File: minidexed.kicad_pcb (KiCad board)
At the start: 2 copper layers, 130.8 x 85 mm, 53 parts, among them J1 Audio Out, J2 MIDI In, J3 Raspberry_Pi_2_3, J4 MIDI Thru, J5 MIDI Out, J6 GND TP, SW1 Encoder, SW2 B1, SW3 B2, SW4 B3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

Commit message: rough out tracks
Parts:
- U3: footprint Package_SO:TSSOP-14_4.4x3.6mm_P0.4mm -> Package_SO:TSSOP-14_4.4x5mm_P0.65mm
- moved R2 14.4 mm to (197.5, 107.0)
- moved R5 14.1 mm to (183.2, 107.0)
- moved J6 9.05 mm to (160.3, 104.3)
- moved C15 5.41 mm to (148.6, 73.1)
- moved R4 4.50 mm to (153.5, 73.1)
- moved TP6 4.14 mm to (151.9, 87.5)
- moved TP5 2.34 mm to (143.8, 81.9)
- moved U3 0.92 mm to (125.7, 87.0)
- moved TP8 0.50 mm to (143.0, 88.0)
- moved R3 0.25 mm to (190.3, 107.0)
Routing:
- net +5V: track 0.00 -> 214.1 mm, vias 0 -> 5
- net +3.3V: track 0.00 -> 202.6 mm, vias 0 -> 3
- net /LCD_E: track 0.00 -> 156.8 mm
- net /BTN_1: track 0.00 -> 114.6 mm
- net /BTN_2: track 0.00 -> 96.0 mm
- net /MIDI_RX: track 0.00 -> 89.6 mm
- net /LCD_RS: track 0.00 -> 86.9 mm, vias 0 -> 1
- net /LCD_D4: track 0.00 -> 69.5 mm
- net /MIDI_TX: track 0.00 -> 69.5 mm
- net /LCD_D5: track 0.00 -> 62.1 mm
- net /LCD_D6: track 0.00 -> 58.1 mm
- net /LCD_D7: track 0.00 -> 52.3 mm, vias 0 -> 1
- net /DAC_A_3V3: track 0.00 -> 51.1 mm, vias 0 -> 2
- net /ENC_A_CLK: track 0.00 -> 39.7 mm
- net /ENC_B_DT: track 0.00 -> 39.2 mm
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- added copper zone on B.Cu, net GND
- added copper zone on F.Cu, net GND
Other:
- rule pad_to_mask_clearance: 0 -> 0.05

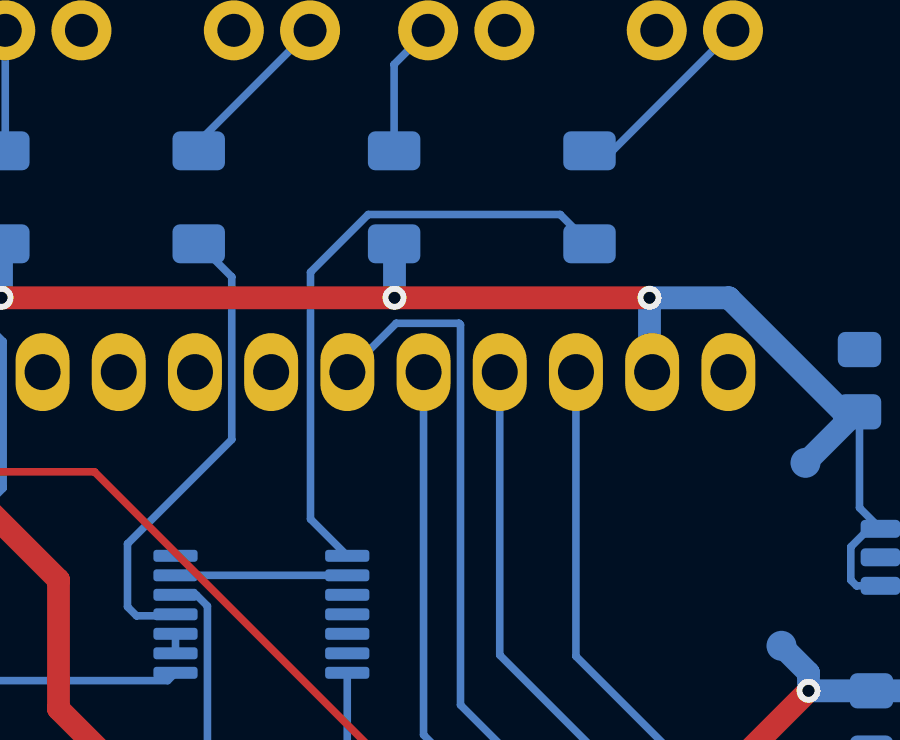
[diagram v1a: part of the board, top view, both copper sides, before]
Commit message: add image errors
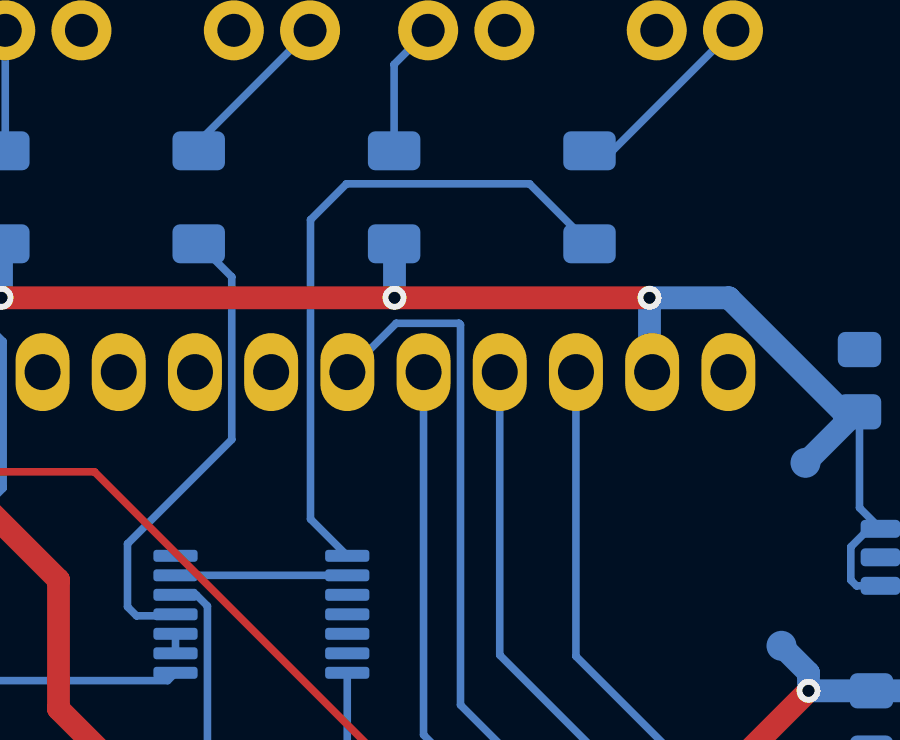
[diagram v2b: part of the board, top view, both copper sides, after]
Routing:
- net Net-(R11-Pad2): track 20.5 -> 22.3 mm
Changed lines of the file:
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@@
   (segment (start 124.675 75.70092) (end 124.675 81.125) (width 0.254) (layer "B.Cu") (net 57))
   (segment (start 121.5 87) (end 122.75 87) (width 0.254) (layer "B.Cu") (net 57))
-  (segment (start 129.223039 73.623) (end 127.3 75.546039) (width 0.254) (layer "B.Cu") (net 58))
-  (segment (start 136.6 74.6) (end 135.623 73.623) (width 0.254) (layer "B.Cu") (net 58))
-  (segment (start 127.3 75.546039) (end 127.3 83.775) (width 0.254) (layer "B.Cu") (net 58))
-  (segment (start 127.3 83.775) (end 128.525 85) (width 0.254) (layer "B.Cu") (net 58))
-  (segment (start 135.623 73.623) (end 129.223039 73.623) (width 0.254) (layer "B.Cu") (net 58))
+  (segment (start 127.3 73.8) (end 128.5 72.6) (width 0.254) (layer "B.Cu") (net 58))
+  (segment (start 127.3 83.775) (end 127.3 73.8) (width 0.254) (layer "B.Cu") (net 58))
+  (segment (start 128.5 72.6) (end 134.6 72.6) (width 0.254) (layer "B.Cu") (net 58))
+  (segment (start 134.6 72.6) (end 136.6 74.6) (width 0.254) (layer "B.Cu") (net 58))
+  (segment (start 128.525 85) (end 127.3 83.775) (width 0.254) (layer "B.Cu") (net 58))
   (segment (start 122.8 87.6) (end 122.8 88.25) (width 0.254) (layer "B.Cu") (net 60))
   (segment (start 128.525 85.65) (end 122.8 85.65) (width 0.254) (layer "B.Cu") (net 61))

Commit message: fix gnd issue
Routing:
- net GND: vias 18 -> 13

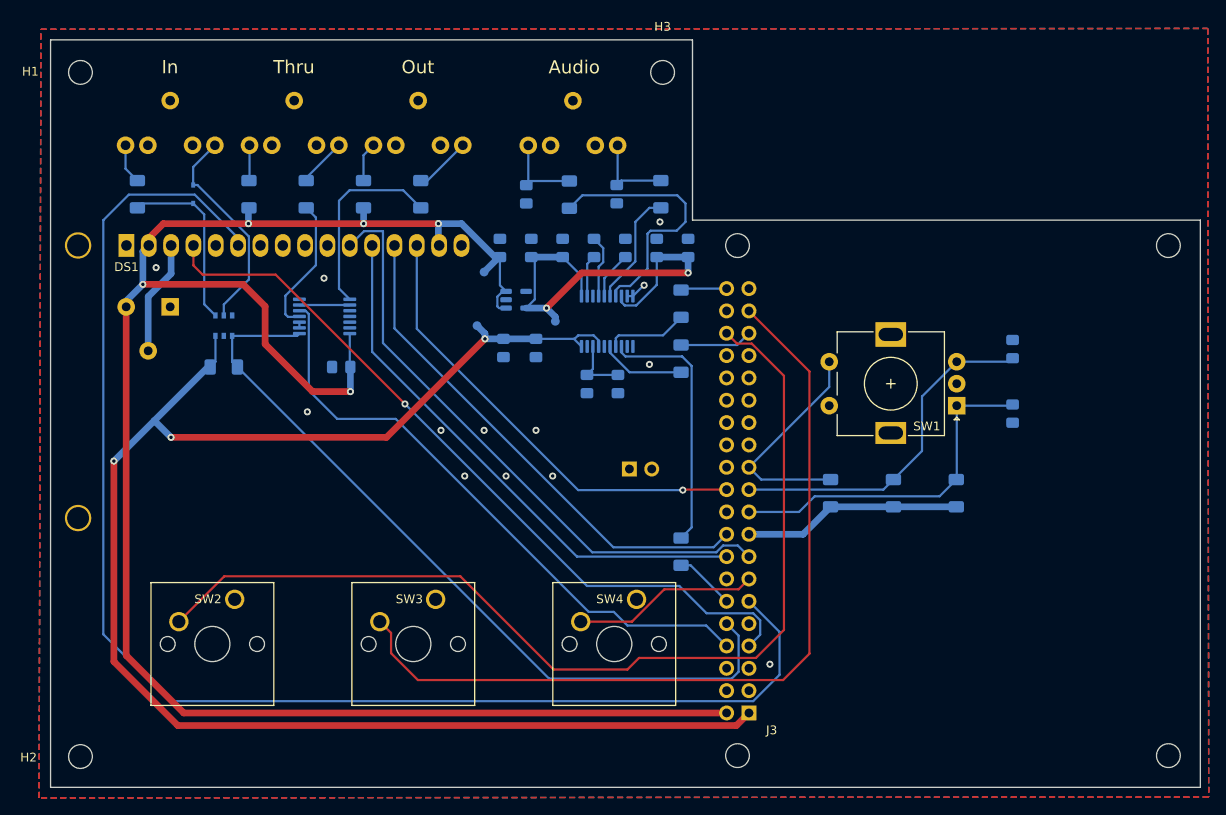
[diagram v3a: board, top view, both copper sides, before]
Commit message: fix missing GND connection
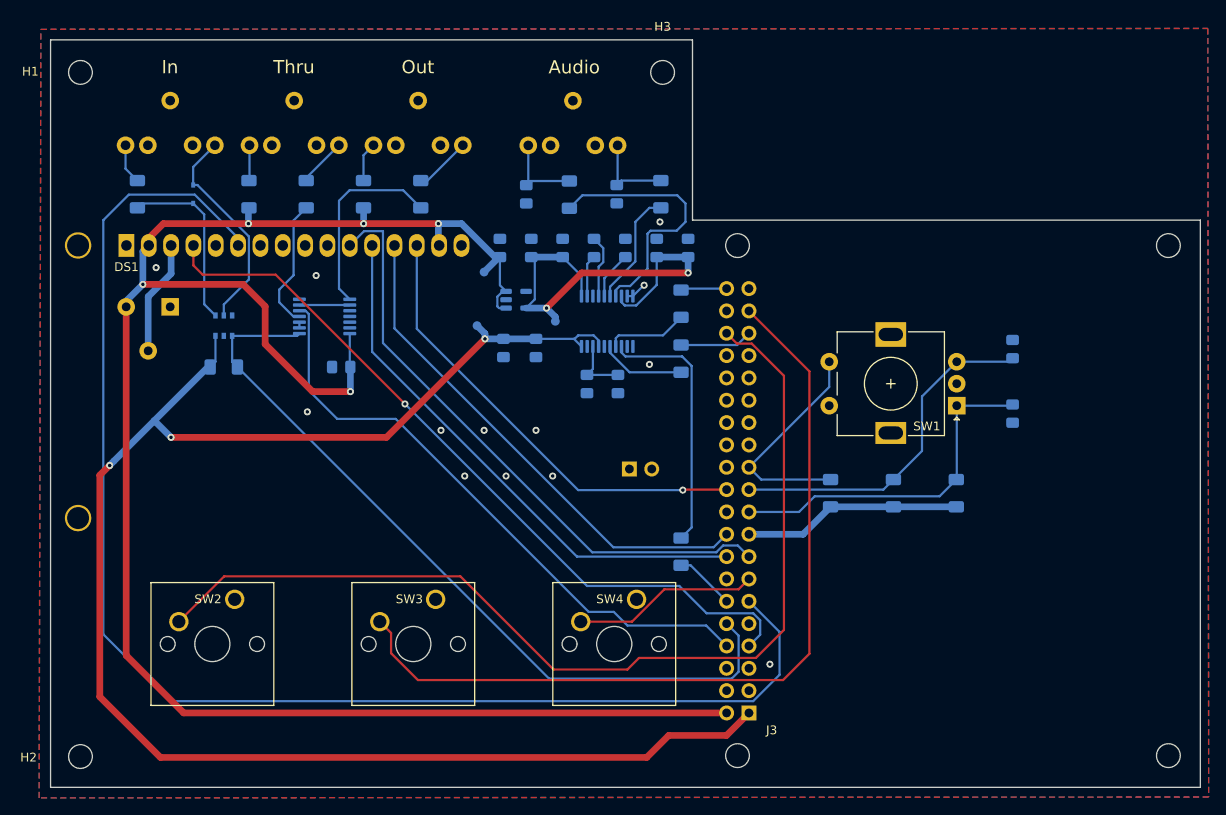
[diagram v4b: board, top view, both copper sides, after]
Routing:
- net +3.3V: track 202.6 -> 210.2 mm
- net Net-(R10-Pad2): track 15.7 -> 15.0 mm
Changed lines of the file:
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@@
   (segment (start 105 83.3) (end 105 79.5445) (width 0.762) (layer "B.Cu") (net 1))
   (segment (start 103.1 85.86) (end 103.1 85.2) (width 0.762) (layer "B.Cu") (net 1))
+  (via (at 124.7 82.3) (size 0.8) (drill 0.4) (layers "F.Cu" "B.Cu") (free) (net 2))
   (via (at 162 83.4) (size 0.8) (drill 0.4) (layers "F.Cu" "B.Cu") (free) (net 2))
   (via (at 151.6 105.1) (size 0.8) (drill 0.4) (layers "F.Cu" "B.Cu") (free) (net 2))
@@
   (via (at 141.6 105.1) (size 0.8) (drill 0.4) (layers "F.Cu" "B.Cu") (free) (net 2))
   (via (at 146.3 105.1) (size 0.8) (drill 0.4) (layers "F.Cu" "B.Cu") (free) (net 2))
-  (via (at 125.6 82.6) (size 0.8) (drill 0.4) (layers "F.Cu" "B.Cu") (free) (net 2))
   (via (at 138.9 99.9) (size 0.8) (drill 0.4) (layers "F.Cu" "B.Cu") (free) (net 2))
   (segment (start 160.725 84.6375) (end 160.075 84.6375) (width 0.254) (layer "B.Cu") (net 2))
@@
   (segment (start 163.43333 80.2) (end 167 80.2) (width 0.762) (layer "B.Cu") (net 3))
   (segment (start 154.875 82.341668) (end 152.733332 80.2) (width 0.254) (layer "B.Cu") (net 3))
+  (segment (start 173.9184 132.0424) (end 171.3608 134.6) (width 0.762) (layer "F.Cu") (net 4))
+  (segment (start 101.2265 103.9) (end 101.2 103.9) (width 0.762) (layer "F.Cu") (net 4))
+  (segment (start 164.8 134.6) (end 162.3 137.1) (width 0.762) (layer "F.Cu") (net 4))
   (segment (start 132.7 100.7) (end 143.9 89.5) (width 0.762) (layer "F.Cu") (net 4))
-  (segment (start 173.9184 132.0424) (end 172.4874 133.4734) (width 0.762) (layer "F.Cu") (net 4))
-  (segment (start 101.7 126.2) (end 108.9734 133.4734) (width 0.762) (layer "F.Cu") (net 4))
-  (segment (start 101.7 126.2) (end 101.7 103.4) (width 0.762) (layer "F.Cu") (net 4))
-  (segment (start 172.4874 133.4734) (end 108.9734 133.4734) (width 0.762) (layer "F.Cu") (net 4))
+  (segment (start 101.2 103.9) (end 100.1 105) (width 0.762) (layer "F.Cu") (net 4))
+  (segment (start 100.1 130.2) (end 100.1 105) (width 0.762) (layer "F.Cu") (net 4))
+  (segment (start 162.3 137.1) (end 107 137.1) (width 0.762) (layer "F.Cu") (net 4))
+  (segment (start 171.3608 134.6) (end 164.8 134.6) (width 0.762) (layer "F.Cu") (net 4))
+  (segment (start 107 137.1) (end 100.1 130.2) (width 0.762) (layer "F.Cu") (net 4))
   (segment (start 108.2 100.7) (end 132.7 100.7) (width 0.762) (layer "F.Cu") (net 4))
   (via (at 108.2 100.7) (size 0.8) (drill 0.4) (layers "F.Cu" "B.Cu") (net 4))
-  (via (at 101.7 103.4) (size 0.8) (drill 0.4) (layers "F.Cu" "B.Cu") (net 4))
+  (via (at 101.2265 103.9) (size 0.8) (drill 0.4) (layers "F.Cu" "B.Cu") (net 4))
   (via (at 143.9 89.5) (size 0.8) (drill 0.4) (layers "F.Cu" "B.Cu") (net 4))
   (segment (start 113.25 89.16) (end 113.25 92.1) (width 0.254) (layer "B.Cu") (net 4))
@@
   (segment (start 106.3 98.8) (end 112.4 92.7) (width 0.762) (layer "B.Cu") (net 4))
   (segment (start 146 89.5) (end 149.7 89.5) (width 0.762) (layer "B.Cu") (net 4))
+  (segment (start 101.7 103.4) (end 101.2265 103.8735) (width 0.762) (layer "B.Cu") (net 4))
   (segment (start 190.35 108.6) (end 197.5 108.6) (width 0.762) (layer "B.Cu") (net 4))
+  (segment (start 101.2265 103.8735) (end 101.2265 103.9) (width 0.762) (layer "B.Cu") (net 4))
   (segment (start 183.2 108.6) (end 190.35 108.6) (width 0.762) (layer "B.Cu") (net 4))
   (segment (start 143.9 88.9) (end 143 88) (width 0.762) (layer "B.Cu") (net 4))
@@
   (segment (start 158.775 89.425131) (end 158.775 90.3625) (width 0.254) (layer "B.Cu") (net 56))
   (segment (start 159.100131 89.1) (end 158.775 89.425131) (width 0.254) (layer "B.Cu") (net 56))
-  (segment (start 121.2 84.6) (end 121.2 86.7) (width 0.254) (layer "B.Cu") (net 57))
-  (segment (start 121.2 86.7) (end 121.5 87) (width 0.254) (layer "B.Cu") (net 57))
-  (segment (start 123.57408 74.6) (end 124.675 75.70092) (width 0.254) (layer "B.Cu") (net 57))
-  (segment (start 124.675 81.125) (end 121.2 84.6) (width 0.254) (layer "B.Cu") (net 57))
-  (segment (start 124.675 75.70092) (end 124.675 81.125) (width 0.254) (layer "B.Cu") (net 57))
-  (segment (start 121.5 87) (end 122.75 87) (width 0.254) (layer "B.Cu") (net 57))
+  (segment (start 120.5 83.9) (end 120.5 85.341369) (width 0.254) (layer "B.Cu") (net 57))
+  (segment (start 122.135 76.03908) (end 122.135 82.265) (width 0.254) (layer "B.Cu") (net 57))
+  (segment (start 120.5 85.341369) (end 122.108631 86.95) (width 0.254) (layer "B.Cu") (net 57))
+  (segment (start 122.135 82.265) (end 120.5 83.9) (width 0.254) (layer "B.Cu") (net 57))
+  (segment (start 123.57408 74.6) (end 122.135 76.03908) (width 0.254) (layer "B.Cu") (net 57))
+  (segment (start 122.108631 86.95) (end 122.8 86.95) (width 0.254) (layer "B.Cu") (net 57))
   (segment (start 127.3 73.8) (end 128.5 72.6) (width 0.254) (layer "B.Cu") (net 58))
   (segment (start 127.3 83.775) (end 127.3 73.8) (width 0.254) (layer "B.Cu") (net 58))
@@
   (segment (start 122.8 87.6) (end 122.8 88.25) (width 0.254) (layer "B.Cu") (net 60))
   (segment (start 128.525 85.65) (end 122.8 85.65) (width 0.254) (layer "B.Cu") (net 61))
-  (zone (net 2) (net_name "GND") (layers F&B.Cu) (hatch edge 0.508)
-    (connect_pads (clearance 0.508))
+  (zone (net 2) (net_name "GND") (layer "F.Cu") (hatch edge 0.508)
+    (connect_pads (clearance 0.254))
     (min_thickness 0.254) (filled_areas_thickness no)
     (fill yes (thermal_gap 0.508) (thermal_bridge_width 0.508))
@@
     )
   )
-  (zone (net 2) (net_name "GND") (layers F&B.Cu) (hatch edge 0.508)
+  (zone (net 2) (net_name "GND") (layer "B.Cu") (hatch edge 0.508)
     (connect_pads (clearance 0.254))
     (min_thickness 0.254) (filled_areas_thickness no)

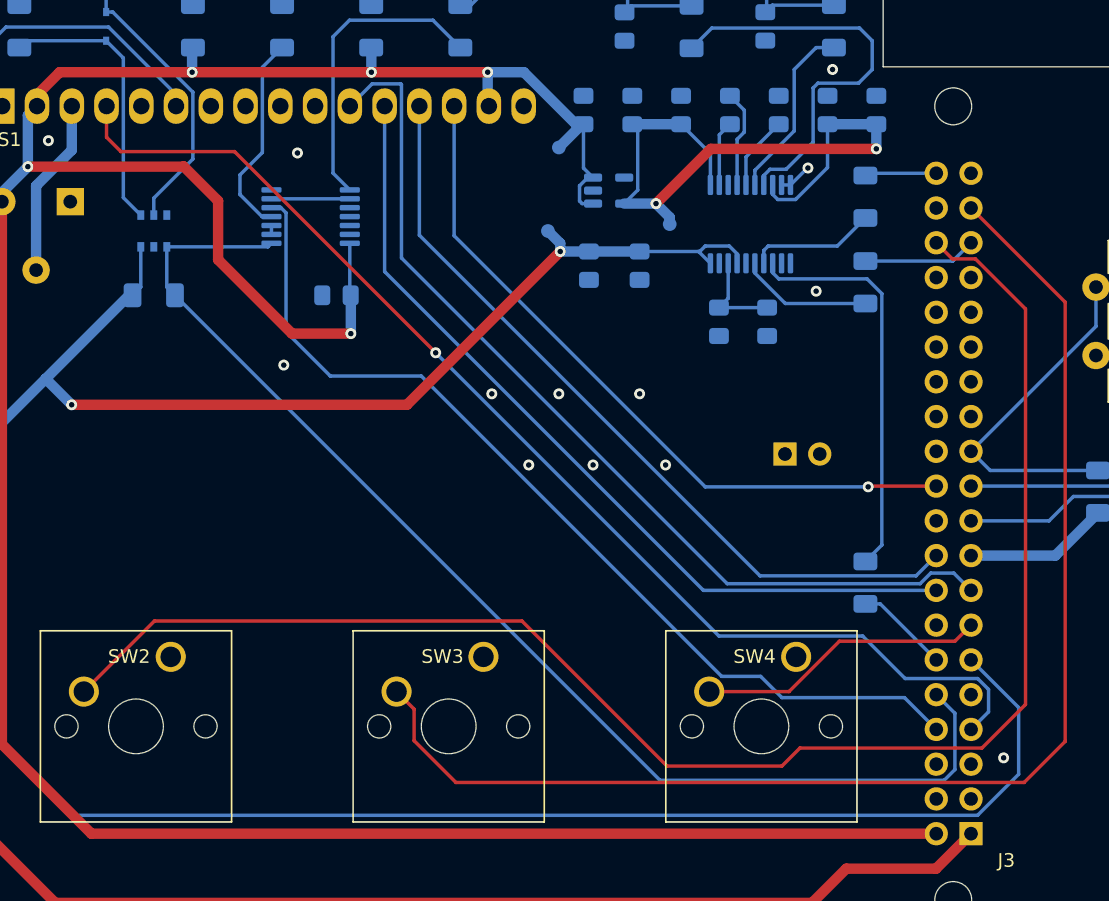
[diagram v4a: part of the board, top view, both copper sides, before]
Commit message: rewire LED
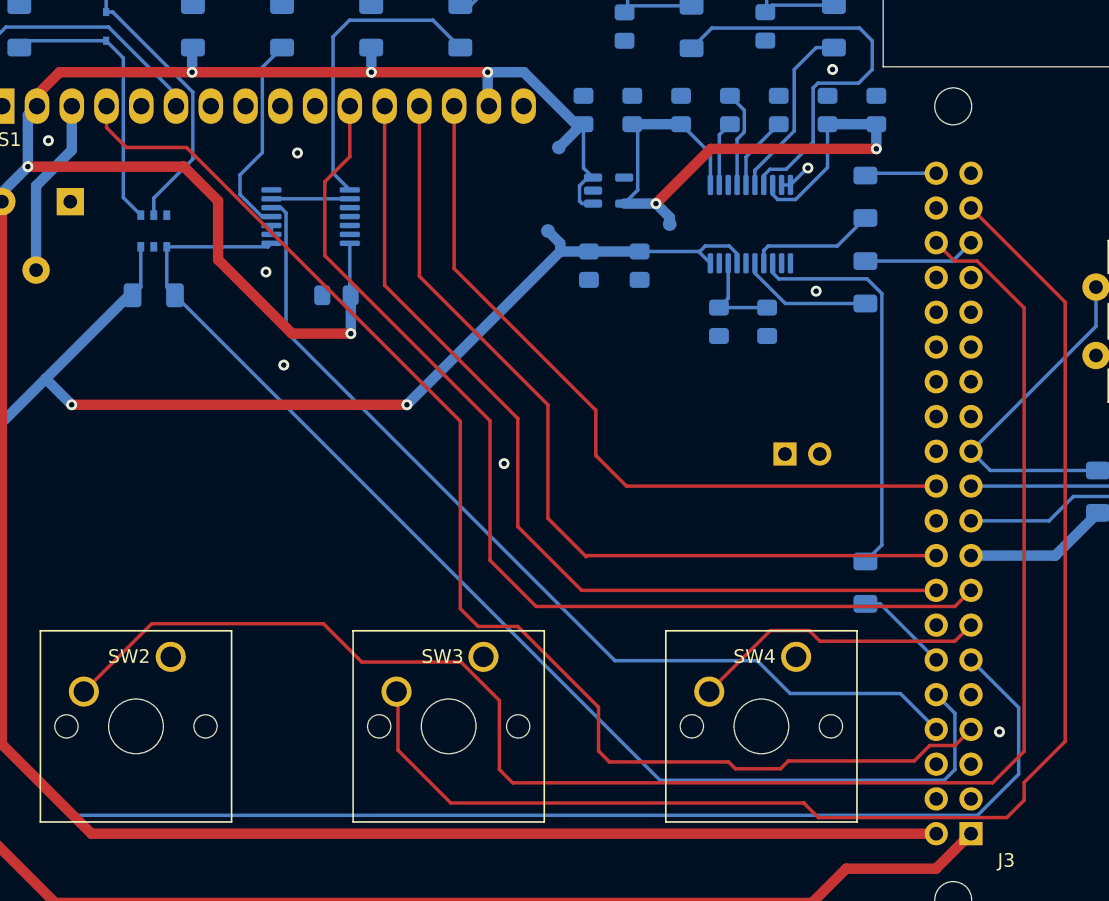
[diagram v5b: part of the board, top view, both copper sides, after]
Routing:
- net /LCD_RS: track 86.9 -> 95.2 mm, vias 1 -> 0
- net /LCD_D4: track 69.5 -> 76.0 mm
- net /BTN_1: track 114.6 -> 120.3 mm
- net /LCD_D6: track 58.1 -> 63.6 mm
- net /LCD_D5: track 62.1 -> 67.3 mm
- net /BTN_2: track 96.0 -> 100.0 mm
- net /LCD_D7: track 52.3 -> 55.6 mm, vias 1 -> 0
- net /BTN_3: track 21.1 -> 21.8 mm
- net GND: vias 13 -> 9

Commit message: update opto footprint
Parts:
- C16: value 0.1uf -> 100nf
- U4: footprint Package_SO:TSOP-6_1.65x3.05mm_P0.95mm -> SOP-6_6.5x7.12mm_P2.54mm:SOP-6_6.5x7.12mm_P2.54mm
- moved R12 4.98 mm to (113.3, 97.6)
- moved RV1 4.30 mm to (103.9, 86.8)
- moved U4 1.42 mm to (113.3, 89.1)
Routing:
- net /LCD_E: track 156.8 -> 82.3 mm
- net /MIDI_TX: track 69.5 -> 94.2 mm
- net /MIDI_RX: track 89.6 -> 104.3 mm
- net /BTN_3: track 21.8 -> 31.2 mm, vias 0 -> 1
- net +5V: track 214.1 -> 221.6 mm, vias 5 -> 4
- net /LCD_RS: track 95.2 -> 90.0 mm
- net Net-(D1-Pad2): track 24.5 -> 20.2 mm
- net Net-(DS1-Pad3): track 13.1 -> 17.1 mm
- net Net-(D1-Pad1): track 19.6 -> 17.4 mm
- net +3.3V: track 210.2 -> 211.7 mm, vias 3 -> 2
- net Net-(R4-Pad1): track 30.5 -> 29.0 mm
- net /BTN_1: track 120.3 -> 119.5 mm
- net GND: vias 9 -> 12

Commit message: export files
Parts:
- moved H1 3.50 mm to (97.9, 62.7)
- moved H3 3.50 mm to (164.1, 62.7)
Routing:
- net +5V: track 221.6 -> 227.8 mm
- net /BTN_2: track 100.0 -> 101.0 mm
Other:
- board size 130.8 x 85 mm -> 130.8 x 81.5 mm

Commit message: organize build files
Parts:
- moved R2 8.99 mm to (205.9, 110.2)
- moved C12 8.60 mm to (212.5, 90.8)
- moved C11 8.60 mm to (212.5, 97.9)
- moved R3 7.22 mm to (196.8, 110.2)
- moved SW1 6.82 mm to (204.4, 96.9)
- moved R5 5.55 mm to (187.8, 110.2)
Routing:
- net /ENC_B_DT: track 39.2 -> 54.0 mm
- net /ENC_A_CLK: track 39.7 -> 54.1 mm
- net /ENC_SW: track 25.6 -> 33.4 mm
- net +3.3V: track 211.7 -> 218.8 mm
- net GND: vias 12 -> 11
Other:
- board text added: "20240727"
- board text added: "Every idea is a waveform waiting to be shaped into something extraordinary. Embrace the frequencies of your imagination. Let your innovations resonate with harmony. - The Algorithm"
- board text added: "MIDI"
- board text added: "MINIDEXED"
- board text added: "MiniDexed PCB"
- board text added: "Trust the algorithm"
- board text added: "h-e.io"
